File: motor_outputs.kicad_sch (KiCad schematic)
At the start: 9 parts, among them J3 1054070

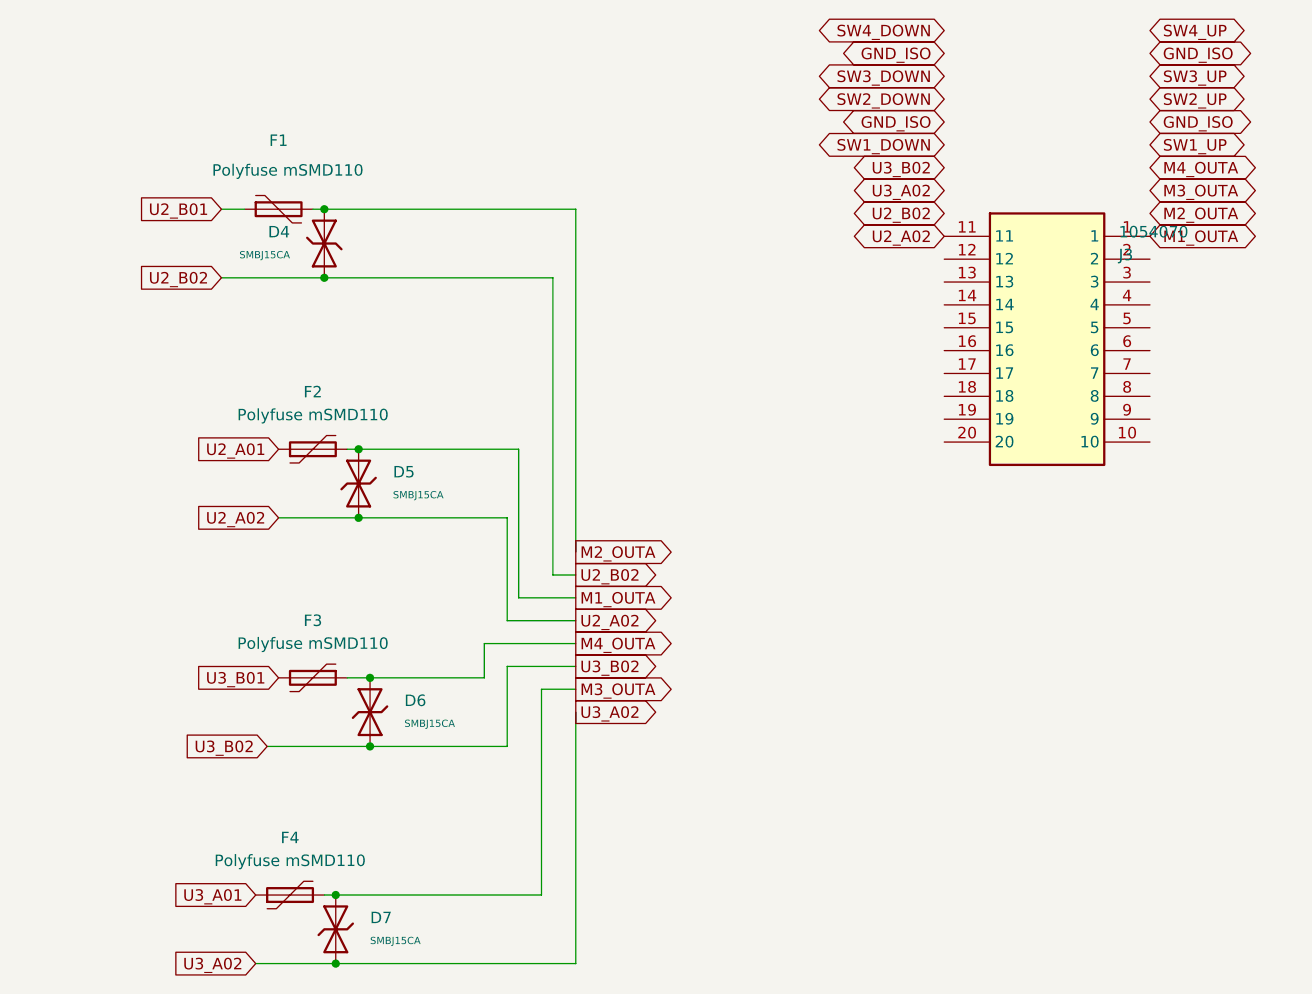
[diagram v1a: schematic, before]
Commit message: Updating routing with new terminal block
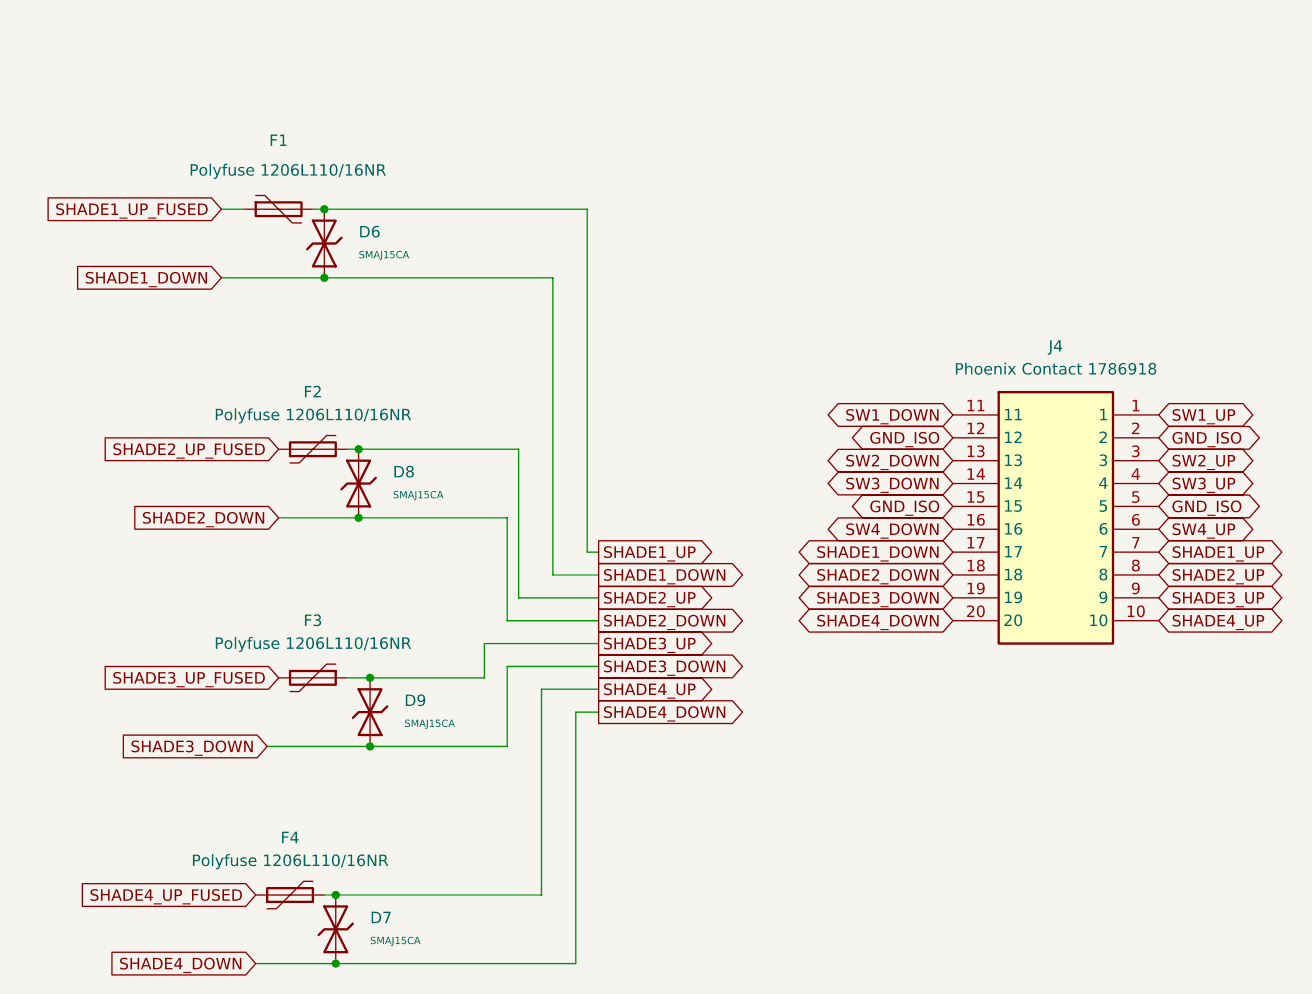
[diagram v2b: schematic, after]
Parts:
- removed J3: 1054070, 1054070:1054070, symbol 1054070:1054070
- added J4: Phoenix Contact 1786918, barn_shade_controller:Phoenix Contact 1786918, symbol New_Library:Phoenix Contact 1786918
- D6: renamed from D4; value SMBJ15CA -> SMAJ15CA; footprint PCM_JLCPCB:D_SMB -> Diode_SMD:D_SMA; symbol PCM_JLCPCB-Diodes:TVS-Bi,SMBJ15CA -> PCM_JLCPCB-Diodes:TVS-Bi,SMAJ15CA; LCSC C19077570 -> C223985; Manufacturer hongjiacheng -> Littelfuse; Part SMBJ15CA -> SMAJ15CA; Price 0.048USD -> (none); Stock 21004 -> 25505
- D7: value SMBJ15CA -> SMAJ15CA; footprint PCM_JLCPCB:D_SMB -> Diode_SMD:D_SMA; symbol PCM_JLCPCB-Diodes:TVS-Bi,SMBJ15CA -> PCM_JLCPCB-Diodes:TVS-Bi,SMAJ15CA; LCSC C19077570 -> C223985; Manufacturer hongjiacheng -> Littelfuse; Part SMBJ15CA -> SMAJ15CA; Price 0.048USD -> (none); Stock 21004 -> 25505
- D8: renamed from D5; value SMBJ15CA -> SMAJ15CA; footprint PCM_JLCPCB:D_SMB -> Diode_SMD:D_SMA; symbol PCM_JLCPCB-Diodes:TVS-Bi,SMBJ15CA -> PCM_JLCPCB-Diodes:TVS-Bi,SMAJ15CA; LCSC C19077570 -> C223985; Manufacturer hongjiacheng -> Littelfuse; Part SMBJ15CA -> SMAJ15CA; Price 0.048USD -> (none); Stock 21004 -> 25505
- D9: renamed from D6; value SMBJ15CA -> SMAJ15CA; footprint PCM_JLCPCB:D_SMB -> Diode_SMD:D_SMA; symbol PCM_JLCPCB-Diodes:TVS-Bi,SMBJ15CA -> PCM_JLCPCB-Diodes:TVS-Bi,SMAJ15CA; LCSC C19077570 -> C223985; Manufacturer hongjiacheng -> Littelfuse; Part SMBJ15CA -> SMAJ15CA; Price 0.048USD -> (none); Stock 21004 -> 25505
- F1, F2, F3, F4: value Polyfuse mSMD110 -> Polyfuse 1206L110/16NR; footprint Fuse:Fuse_1812_4532Metric -> Fuse:Fuse_1206_3216Metric; LCSC C69691 -> C7542961
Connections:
- net GND_ISO: now also J4.12, J4.15, J4.2, J4.5
- net SW1_DOWN: now also J4.11
- net SW1_UP: now also J4.1
- net SW2_DOWN: now also J4.13
- net SW2_UP: now also J4.3
- net SW3_DOWN: now also J4.14
- net SW3_UP: now also J4.4
- net SW4_DOWN: now also J4.16
- net SW4_UP: now also J4.6
- net M1_OUTA renamed SHADE2_UP
- net SHADE2_UP: now also J4.8
- net M2_OUTA renamed SHADE1_UP
- net SHADE1_UP: now also J4.7
- net M3_OUTA renamed SHADE4_UP
- net SHADE4_UP: now also J4.10
- net M4_OUTA renamed SHADE3_UP
- net SHADE3_UP: now also J4.9
- net U2_A01 renamed SHADE2_UP_FUSED
- net U2_A02 renamed SHADE2_DOWN
- net SHADE2_DOWN: now also J4.18
- net U2_B01 renamed SHADE1_UP_FUSED
- net U2_B02 renamed SHADE1_DOWN
- net SHADE1_DOWN: now also J4.17
- net U3_A01 renamed SHADE4_UP_FUSED
- net U3_A02 renamed SHADE4_DOWN
- net SHADE4_DOWN: now also J4.20
- net U3_B01 renamed SHADE3_UP_FUSED
- net U3_B02 renamed SHADE3_DOWN
- net SHADE3_DOWN: now also J4.19
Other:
- moved on the sheet: D6
